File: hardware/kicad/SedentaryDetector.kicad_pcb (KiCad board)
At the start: 2 copper layers, 2 parts, among them J1 ESP32-WROOM-32_2x15, J2 MPU6050_1x8

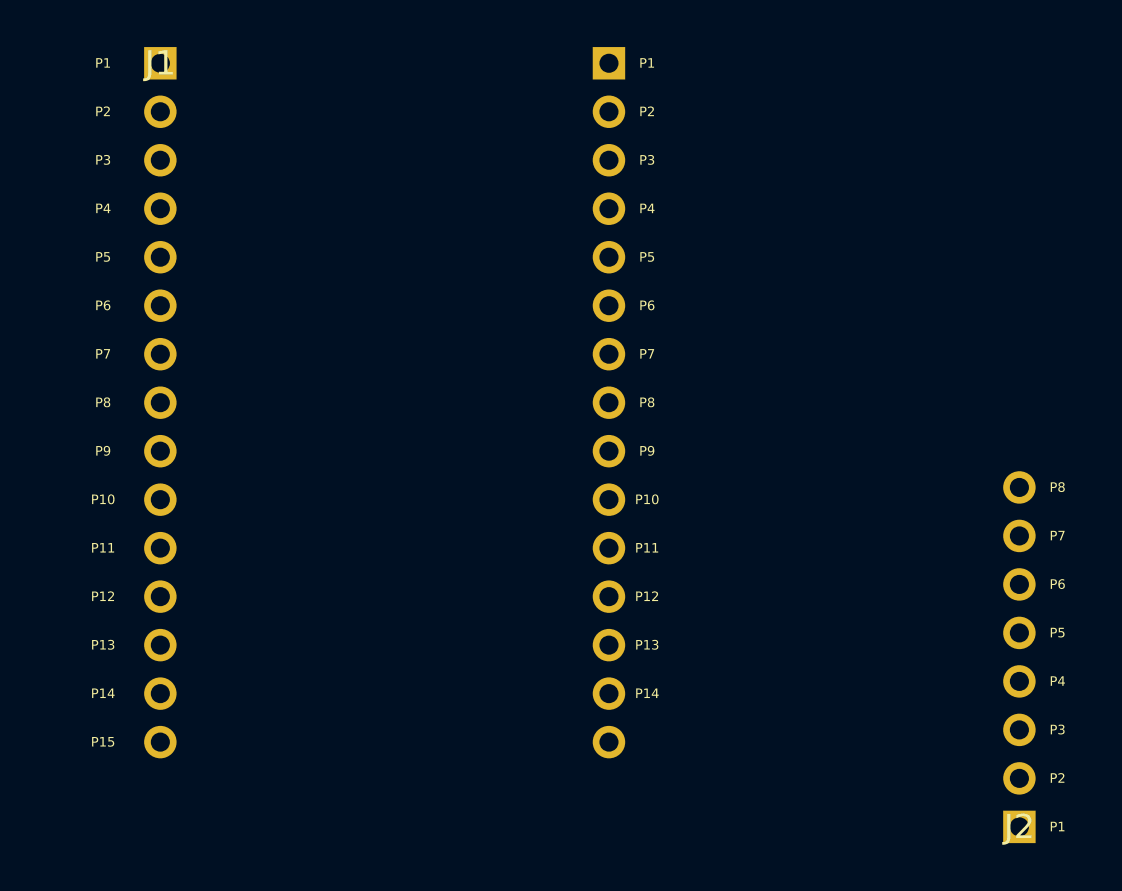
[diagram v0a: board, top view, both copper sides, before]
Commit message: PCB silk: L-P1~L-P15, R-P1~R-P14, J2-P1~J2-P8 format
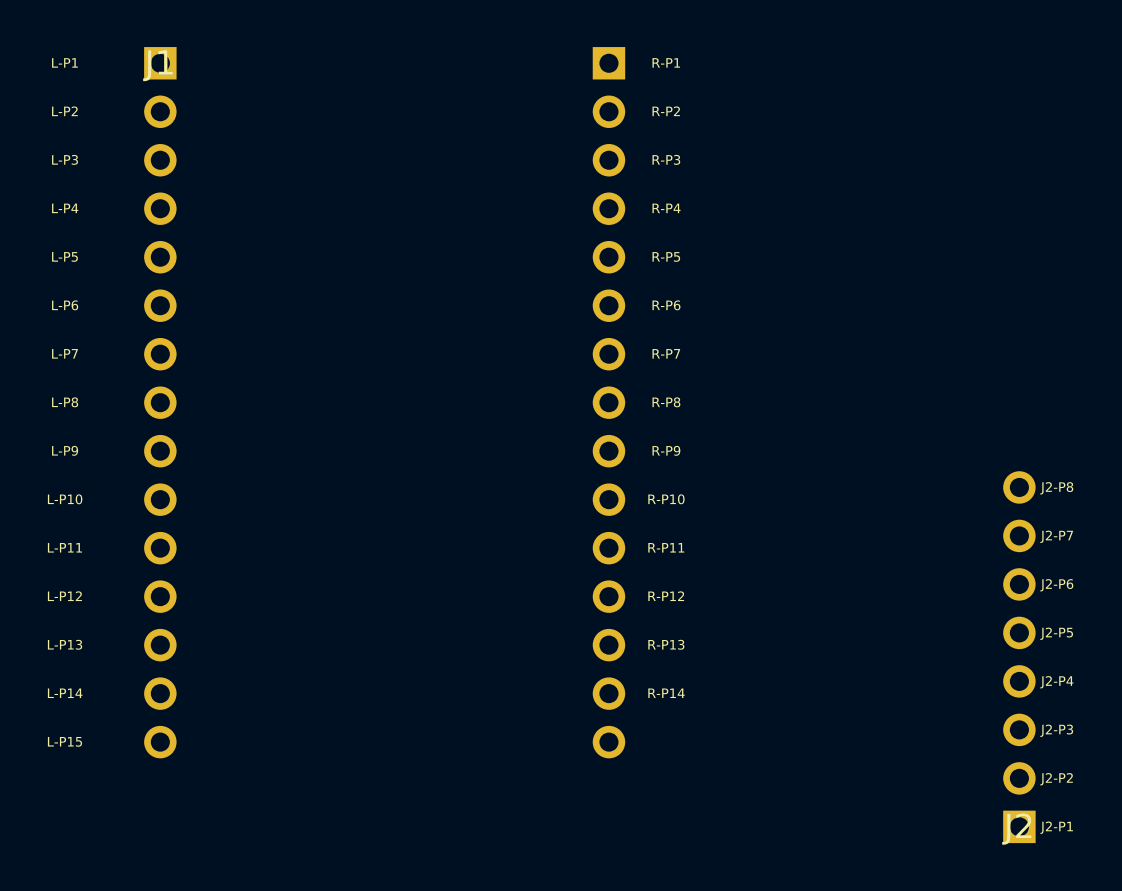
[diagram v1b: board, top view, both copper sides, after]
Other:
- board text added: "J2-P1"
- board text added: "J2-P2"
- board text added: "J2-P3"
- board text added: "J2-P4"
- board text added: "J2-P5"
- board text added: "J2-P6"
- board text added: "J2-P7"
- board text added: "J2-P8"
- board text added: "L-P1"
- board text added: "L-P10"
- board text added: "L-P11"
- board text added: "L-P12"
- board text added: "L-P13"
- board text added: "L-P14"
- board text added: "L-P15"
- board text added: "L-P2"
- board text added: "L-P3"
- board text added: "L-P4"
- board text added: "L-P5"
- board text added: "L-P6"
- board text added: "L-P7"
- board text added: "L-P8"
- board text added: "L-P9"
- board text added: "R-P1"
- board text added: "R-P10"
- board text added: "R-P11"
- board text added: "R-P12"
- board text added: "R-P13"
- board text added: "R-P14"
- board text added: "R-P2"
- board text added: "R-P3"
- board text added: "R-P4"
- board text added: "R-P5"
- board text added: "R-P6"
- board text added: "R-P7"
- board text added: "R-P8"
- board text added: "R-P9"
- board text removed: "P1"
- board text removed: "P10"
- board text removed: "P11"
- board text removed: "P12"
- board text removed: "P13"
- board text removed: "P14"
- board text removed: "P15"
- board text removed: "P2"
- board text removed: "P3"
- board text removed: "P4"
- board text removed: "P5"
- board text removed: "P6"
- board text removed: "P7"
- board text removed: "P8"
- board text removed: "P9"

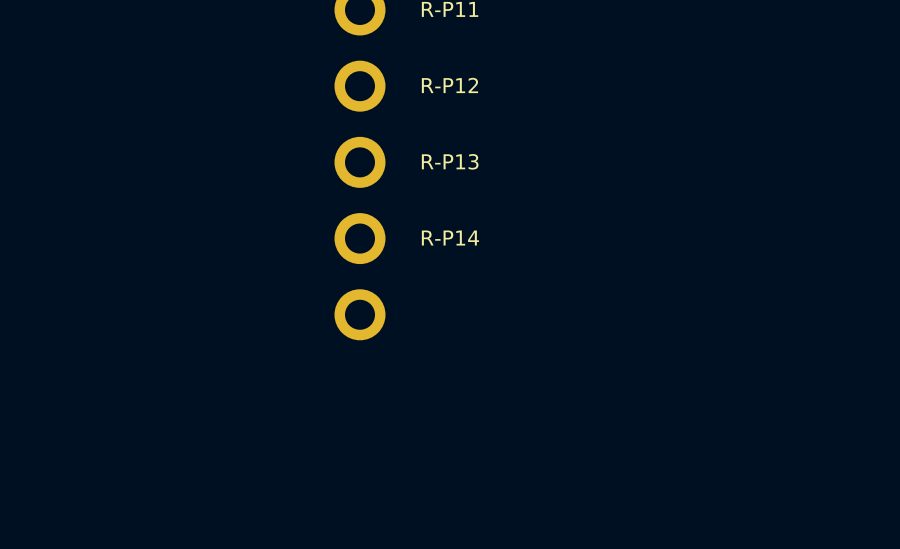
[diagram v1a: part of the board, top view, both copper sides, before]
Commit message: PCB silk: R-P1~R-P15 (both columns 15 labels)
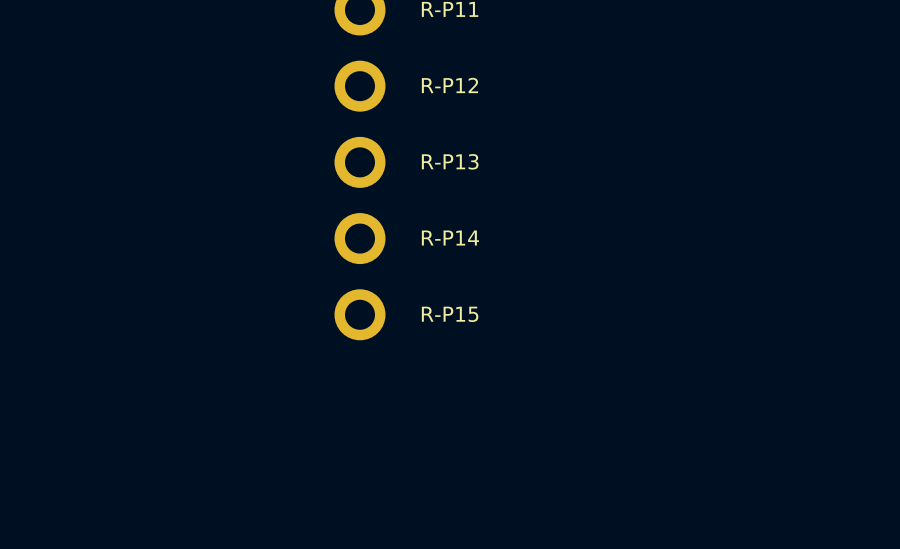
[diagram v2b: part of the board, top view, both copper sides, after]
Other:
- board text added: "R-P15"
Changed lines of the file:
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@@
+		)
+	)
+	(gr_text "R-P15"
+		(at 101.5 164.06 0)
+		(layer "F.SilkS")
+		(effects
+			(font
+				(size 0.5 0.5)
+				(thickness 0.15)
+			)
 		)
 	)

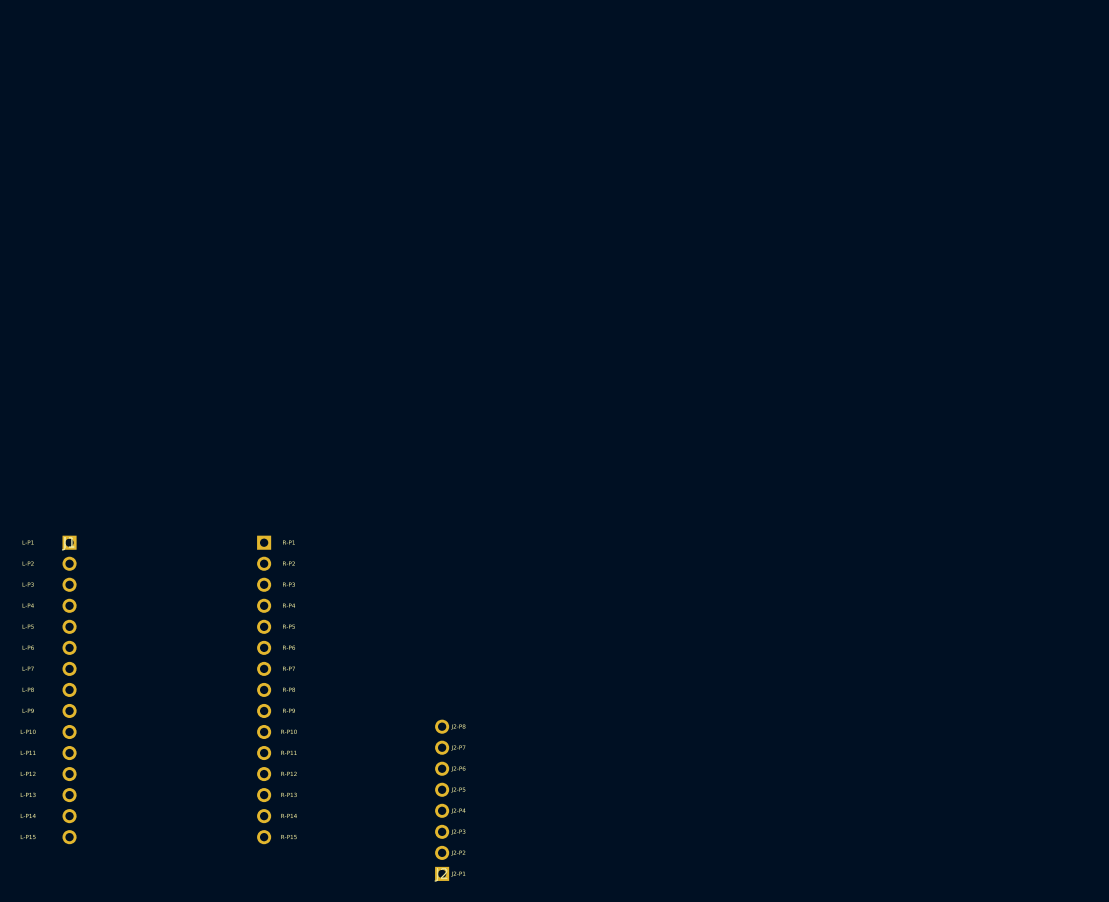
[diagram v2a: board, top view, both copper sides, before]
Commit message: feat(hardware): enlarge board to 100x80mm, correct pin placement
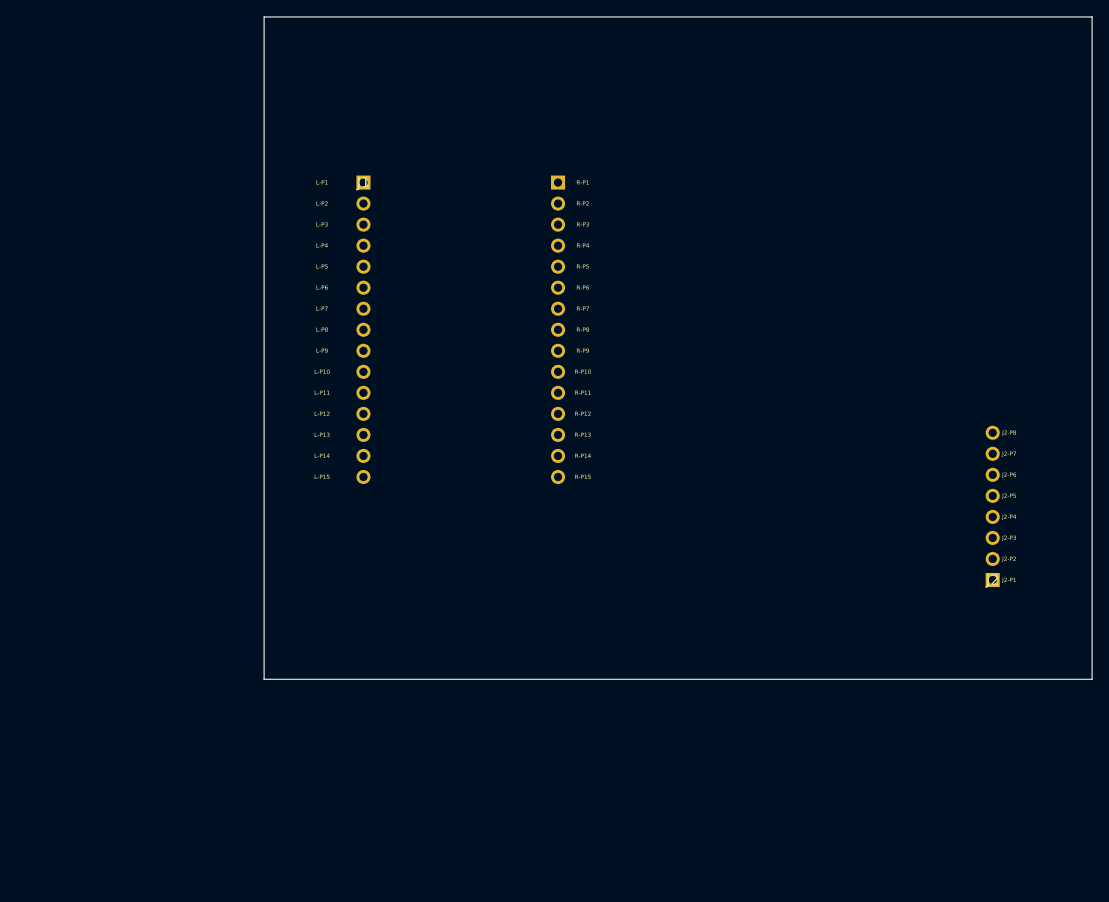
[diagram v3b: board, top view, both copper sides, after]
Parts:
- J1: value ESP32-WROOM-32_2x15 -> ESP32_2x15
- moved J2 75.4 mm to (186.5, 133.0)
- moved J1 56.1 mm to (110.5, 85.0)
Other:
- board outline added: 100 x 80 mm
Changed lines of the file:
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@@
 	(footprint ""
 		(layer "F.Cu")
-		(at 120 168.5)
+		(at 186.5 133)
 		(property "Reference" "J2"
 			(at 0 0 0)
@@
 	(footprint ""
 		(layer "F.Cu")
-		(at 75 128.5)
+		(at 110.5 85)
 		(property "Reference" "J1"
 			(at 0 0 0)
@@
 			)
 		)
-		(property "Value" "ESP32-WROOM-32_2x15"
+		(property "Value" "ESP32_2x15"
 			(at 0 0 0)
 			(layer "F.Fab")
@@
 		)
 		(pad "2" thru_hole circle
-			(at 0 2.539999)
+			(at 0 2.54)
 			(size 1.7 1.7)
 			(drill 1)
@@
 		)
 		(pad "17" thru_hole circle
-			(at 23.5 2.539999)
+			(at 23.5 2.54)
 			(size 1.7 1.7)
 			(drill 1)
@@
 		(embedded_fonts no)
 	)
+	(gr_line
+		(start 98.5 65)
+		(end 198.5 65)
+		(stroke
+			(width 0.1)
+			(type default)
+		)
+		(layer "Edge.Cuts")
+	)
+	(gr_line
+		(start 98.5 145)
+		(end 98.5 65)
+		(stroke
+			(width 0.1)
+			(type default)
+		)
+		(layer "Edge.Cuts")
+	)
+	(gr_line
+		(start 198.5 65)
+		(end 198.5 145)
+		(stroke
+			(width 0.1)
+			(type default)
+		)
+		(layer "Edge.Cuts")
+	)
+	(gr_line
+		(start 198.5 145)
+		(end 98.5 145)
+		(stroke
+			(width 0.1)
+			(type default)
+		)
+		(layer "Edge.Cuts")
+	)
 	(gr_text "L-P1"
-		(at 70 128.5 0)
+		(at 105.5 85 0)
 		(layer "F.SilkS")
 		(effects
@@
 	)
 	(gr_text "L-P2"
-		(at 70 131.039999 0)
+		(at 105.5 87.54 0)
 		(layer "F.SilkS")
 		(effects
@@
 	)
 	(gr_text "L-P3"
-		(at 70 133.58 0)
+		(at 105.5 90.08 0)
 		(layer "F.SilkS")
 		(effects
@@
 	)
 	(gr_text "L-P4"
-		(at 70 136.12 0)
+		(at 105.5 92.62 0)
 		(layer "F.SilkS")
 		(effects
@@
 	)
 	(gr_text "L-P5"
-		(at 70 138.66 0)
+		(at 105.5 95.16 0)
 		(layer "F.SilkS")
 		(effects
@@
 	)
 	(gr_text "L-P6"
-		(at 70 141.2 0)
+		(at 105.5 97.7 0)
 		(layer "F.SilkS")
 		(effects
@@
 	)
 	(gr_text "L-P7"
-		(at 70 143.74 0)
+		(at 105.5 100.24 0)
 		(layer "F.SilkS")
 		(effects
@@
 	)
 	(gr_text "L-P8"
-		(at 70 146.28 0)
+		(at 105.5 102.78 0)
 		(layer "F.SilkS")
 		(effects
@@
 	)
 	(gr_text "L-P9"
-		(at 70 148.82 0)
+		(at 105.5 105.32 0)
 		(layer "F.SilkS")
 		(effects
@@
 	)
 	(gr_text "L-P10"
-		(at 70 151.36 0)
+		(at 105.5 107.86 0)
 		(layer "F.SilkS")
 		(effects
@@
 	)
 	(gr_text "L-P11"
-		(at 70 153.9 0)
+		(at 105.5 110.4 0)
 		(layer "F.SilkS")
 		(effects
@@
 	)
 	(gr_text "L-P12"
-		(at 70 156.44 0)
+		(at 105.5 112.94 0)
 		(layer "F.SilkS")
 		(effects
@@
 	)
 	(gr_text "L-P13"
-		(at 70 158.98 0)
+		(at 105.5 115.48 0)
 		(layer "F.SilkS")
 		(effects
@@
 	)
 	(gr_text "L-P14"
-		(at 70 161.52 0)
+		(at 105.5 118.02 0)
 		(layer "F.SilkS")
 		(effects
@@
 	)
 	(gr_text "L-P15"
-		(at 70 164.06 0)
+		(at 105.5 120.56 0)
 		(layer "F.SilkS")
 		(effects
@@
 	)
 	(gr_text "R-P1"
-		(at 101.5 128.5 0)
+		(at 137 85 0)
 		(layer "F.SilkS")
 		(effects
@@
 	)
 	(gr_text "R-P2"
-		(at 101.5 131.039999 0)
+		(at 137 87.54 0)
 		(layer "F.SilkS")
 		(effects
@@
 	)
 	(gr_text "R-P3"
-		(at 101.5 133.58 0)
+		(at 137 90.08 0)
 		(layer "F.SilkS")
 		(effects
@@
 	)
 	(gr_text "R-P4"
-		(at 101.5 136.12 0)
+		(at 137 92.62 0)
 		(layer "F.SilkS")
 		(effects
@@
 	)
 	(gr_text "R-P5"
-		(at 101.5 138.66 0)
+		(at 137 95.16 0)
 		(layer "F.SilkS")
 		(effects
@@
 	)
 	(gr_text "R-P6"
-		(at 101.5 141.2 0)
+		(at 137 97.7 0)
 		(layer "F.SilkS")
 		(effects
@@
 	)
 	(gr_text "R-P7"
-		(at 101.5 143.74 0)
+		(at 137 100.24 0)
 		(layer "F.SilkS")
 		(effects
@@
 	)
 	(gr_text "R-P8"
-		(at 101.5 146.28 0)
+		(at 137 102.78 0)
 		(layer "F.SilkS")
 		(effects
@@
 	)
 	(gr_text "R-P9"
-		(at 101.5 148.82 0)
+		(at 137 105.32 0)
 		(layer "F.SilkS")
 		(effects
@@
 	)
 	(gr_text "R-P10"
-		(at 101.5 151.36 0)
+		(at 137 107.86 0)
 		(layer "F.SilkS")
 		(effects
@@
 	)
 	(gr_text "R-P11"
-		(at 101.5 153.9 0)
+		(at 137 110.4 0)
 		(layer "F.SilkS")
 		(effects
@@
 	)
 	(gr_text "R-P12"
-		(at 101.5 156.44 0)
+		(at 137 112.94 0)
 		(layer "F.SilkS")
 		(effects
@@
 	)
 	(gr_text "R-P13"
-		(at 101.5 158.98 0)
+		(at 137 115.48 0)
 		(layer "F.SilkS")
 		(effects
@@
 	)
 	(gr_text "R-P14"
-		(at 101.5 161.52 0)
+		(at 137 118.02 0)
 		(layer "F.SilkS")
 		(effects
@@
 	)
 	(gr_text "R-P15"
-		(at 101.5 164.06 0)
+		(at 137 120.56 0)
 		(layer "F.SilkS")
 		(effects
@@
 	)
 	(gr_text "J2-P8"
-		(at 122 150.72 0)
+		(at 188.5 115.22 0)
 		(layer "F.SilkS")
 		(effects
@@
 	)
 	(gr_text "J2-P7"
-		(at 122 153.26 0)
+		(at 188.5 117.76 0)
 		(layer "F.SilkS")
 		(effects
@@
 	)
 	(gr_text "J2-P6"
-		(at 122 155.8 0)
+		(at 188.5 120.3 0)
 		(layer "F.SilkS")
 		(effects
@@
 	)
 	(gr_text "J2-P5"
-		(at 122 158.34 0)
+		(at 188.5 122.84 0)
 		(layer "F.SilkS")
 		(effects
@@
 	)
 	(gr_text "J2-P4"
-		(at 122 160.88 0)
+		(at 188.5 125.38 0)
 		(layer "F.SilkS")
 		(effects
@@
 	)
 	(gr_text "J2-P3"
-		(at 122 163.42 0)
+		(at 188.5 127.92 0)
 		(layer "F.SilkS")
 		(effects
@@
 	)
 	(gr_text "J2-P2"
-		(at 122 165.96 0)
+		(at 188.5 130.46 0)
 		(layer "F.SilkS")
 		(effects
@@
 	)
 	(gr_text "J2-P1"
-		(at 122 168.5 0)
-		(layer "F.SilkS")
-		(effects
+		(at 188.5 133 0)
+		(layer "F.SilkS")
+		(effects
